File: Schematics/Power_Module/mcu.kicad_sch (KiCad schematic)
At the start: 38 parts, among them J5 USB_C_Female_USB2_Small, J6 SWD_B, J7 Stack Male Edge Connector, SW1 SW_STM_RESET, SW2 SW_STM_BOOT_MODE, U13 CP2102N-A02-GQFN20R, U14 STM32F103CBT6, U15 ISO1044BDR, U16 W25Q128JVS, Y1 X322516MMB4SI

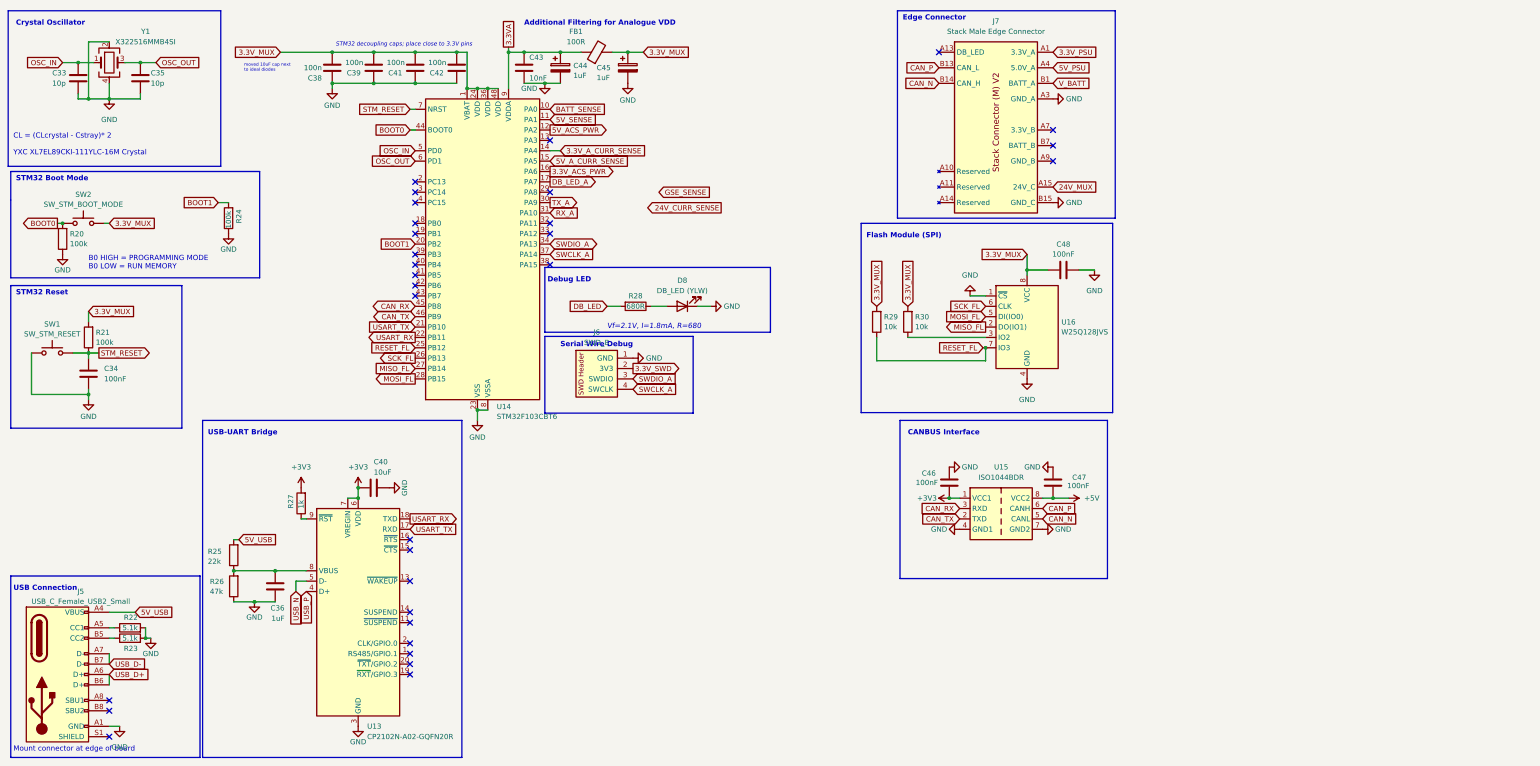
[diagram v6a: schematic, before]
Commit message: major layout progress, still need to place MCU
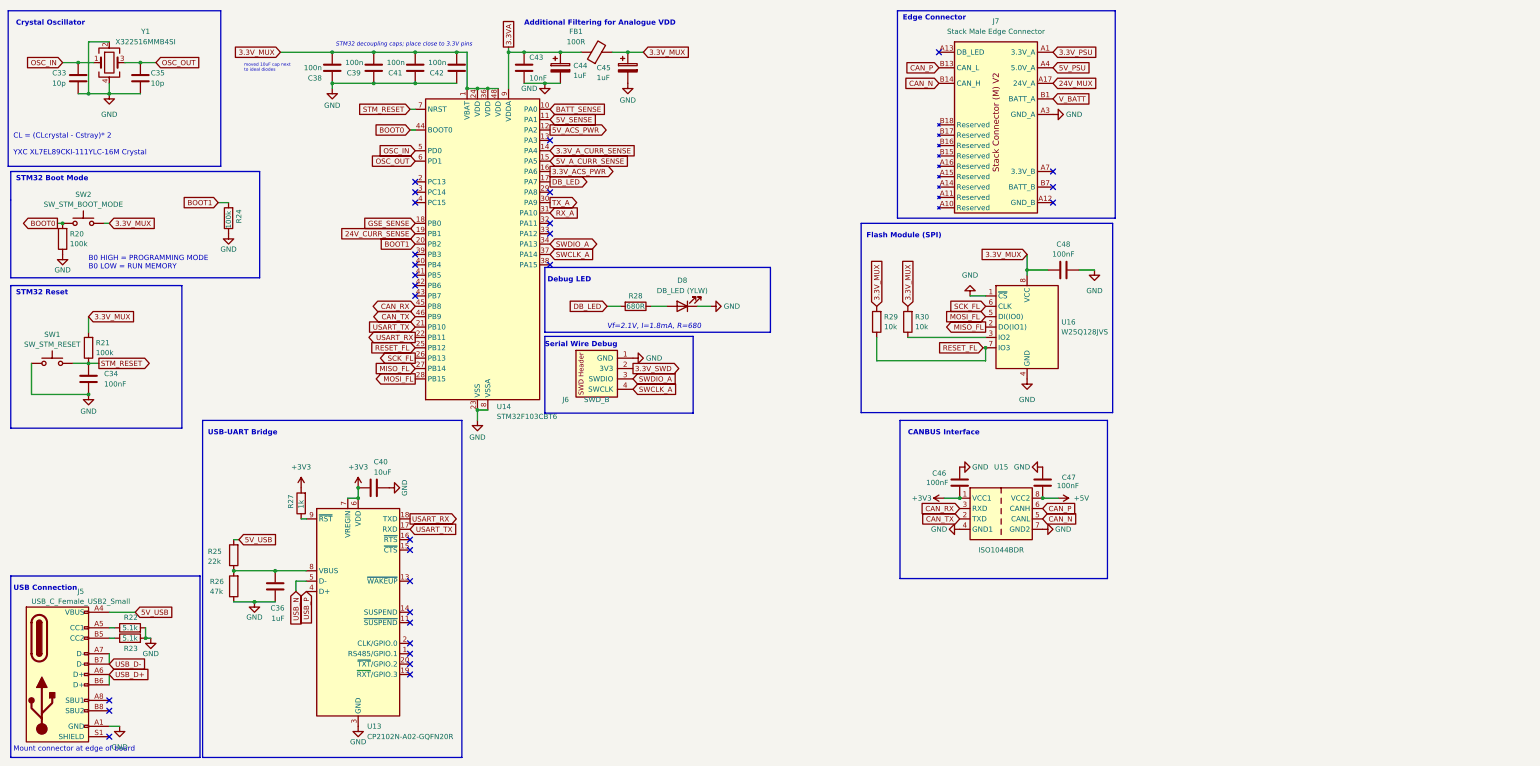
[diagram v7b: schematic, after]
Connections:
- net DB_LED_A is gone; now on net DB_LED: U14.17 (PA7)
- net 24V_CURR_SENSE: now also U14.19 (PB1)
- net 24V_MUX: no longer J7.A15 (24V_C), J7.A16 (24V_C)
- net GND: no longer J7.B15 (GND_C), J7.B16 (GND_C), J7.B17 (GND_C), J7.B18 (GND_C)
- net GSE_SENSE: now also U14.18 (PB0)
- no-connect marks 31 -> 29
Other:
- moved on the sheet: C34, C46, C47, R21, SW1

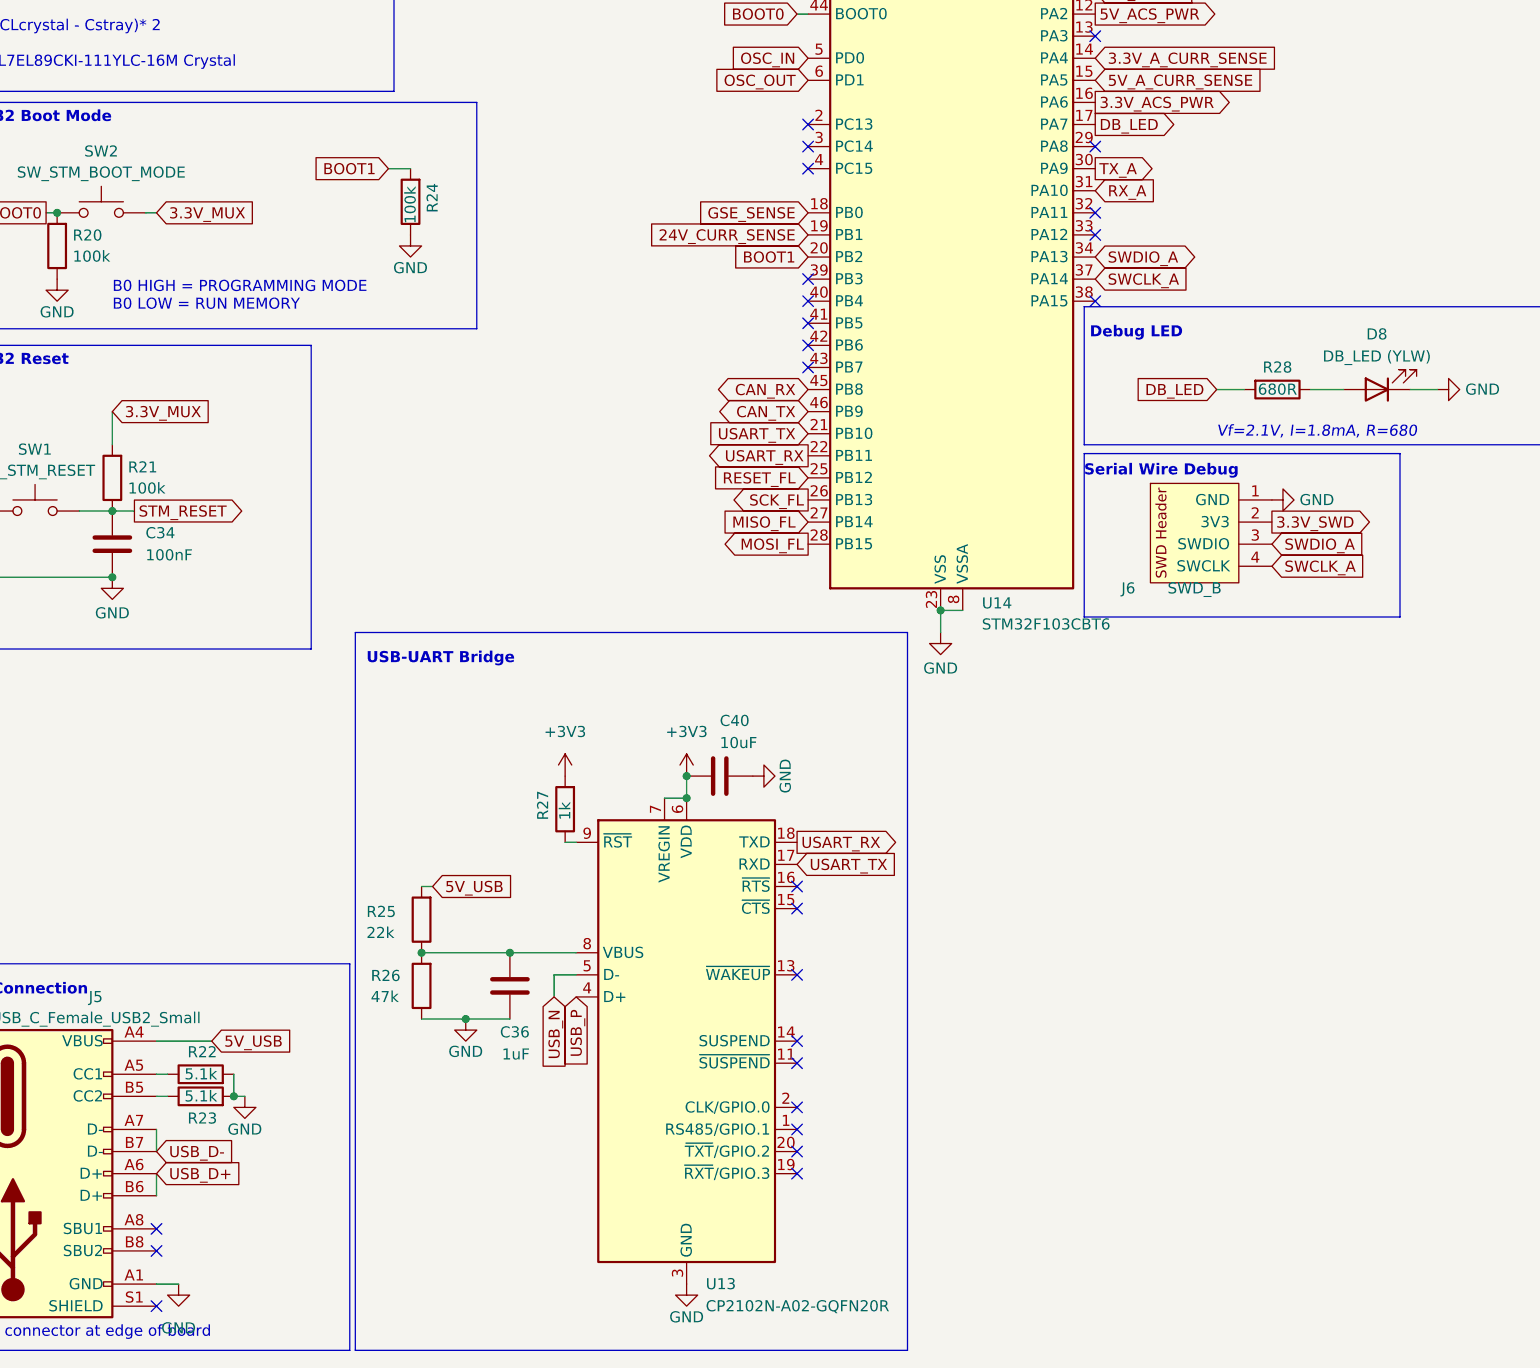
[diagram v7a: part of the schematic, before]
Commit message: continueing layout, confirmed all devices will fix  - need to add bulk rail caps  - fixed issue in oring logic
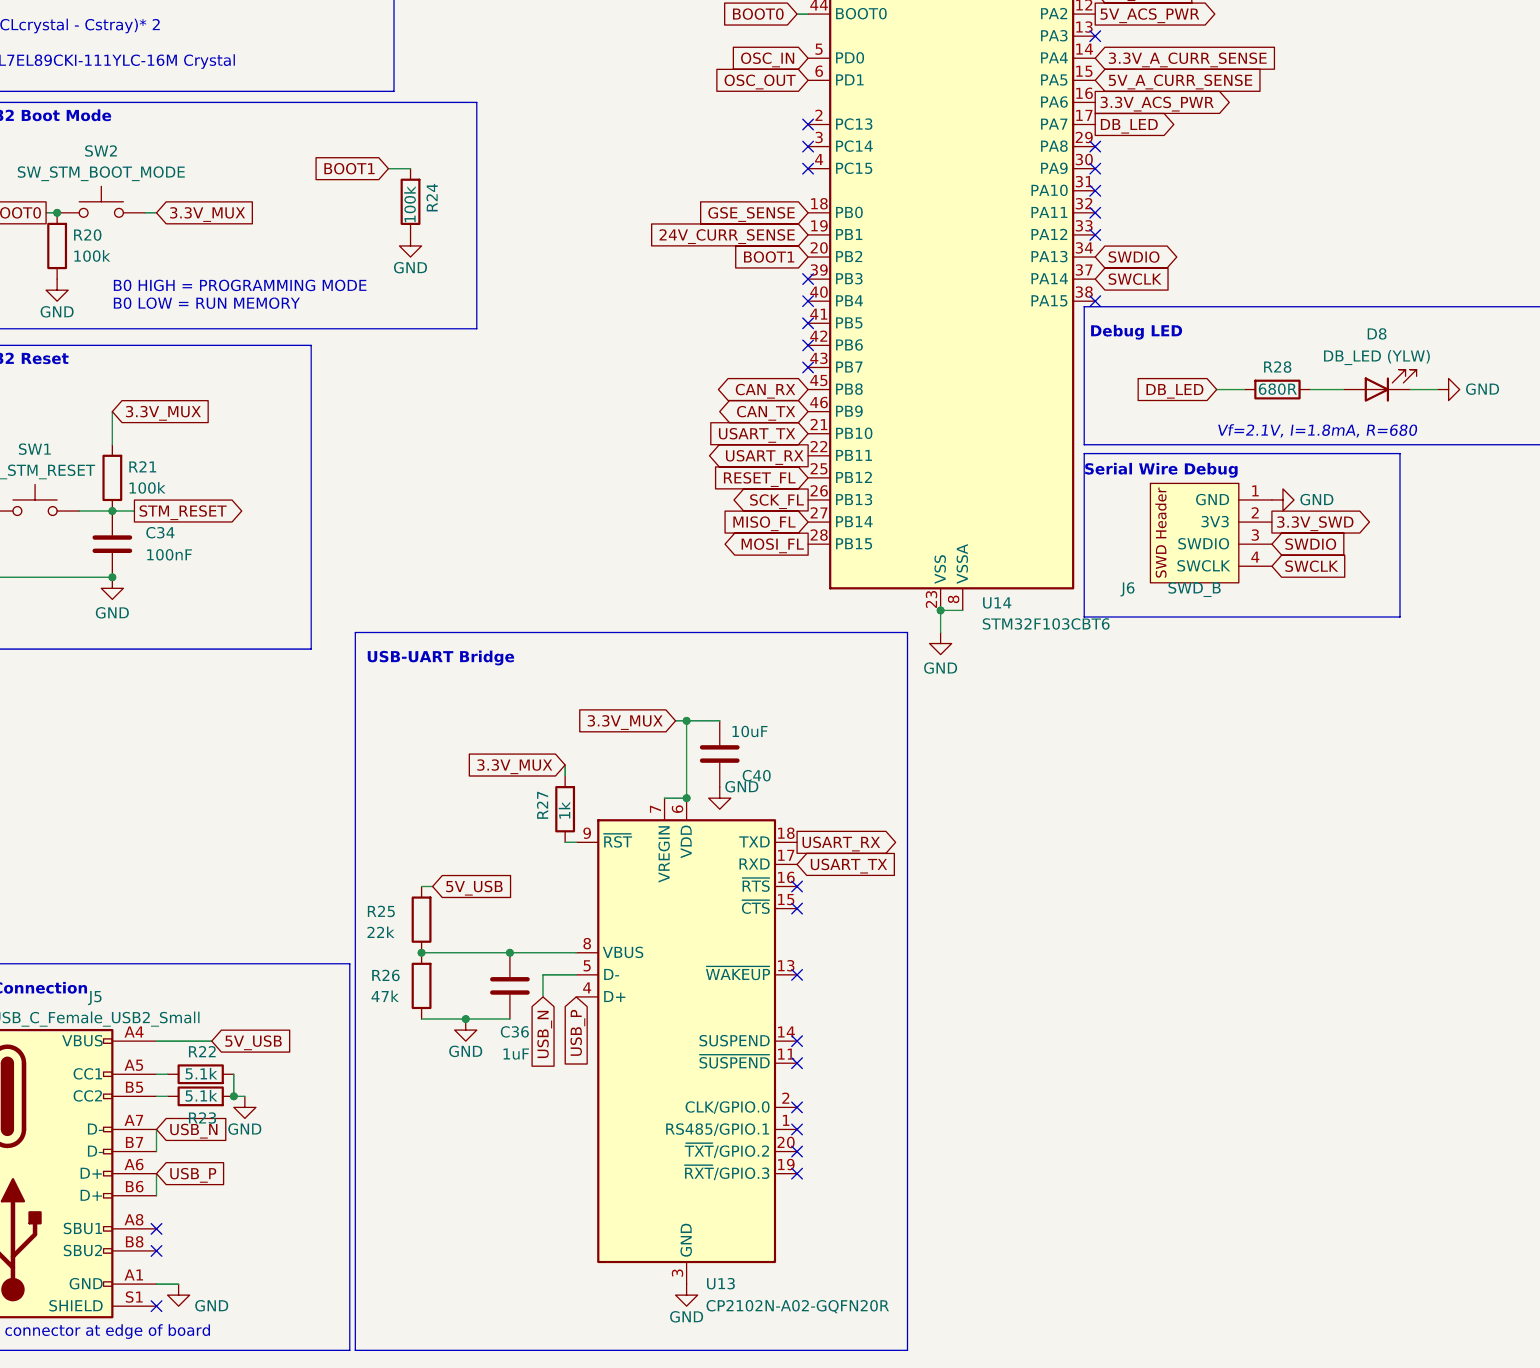
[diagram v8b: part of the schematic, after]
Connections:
- net USB_D+ is gone; now on net USB_P: J5.A6 (D+), J5.B6 (D+)
- net USB_D- is gone; now on net USB_N: J5.A7 (D-), J5.B7 (D-)
- net +3V3: no longer C40.2, R27.2, U13.6 (VDD), U13.7 (VREGIN)
- net 3.3V_MUX: now also C40.1, R27.2, U13.6 (VDD), U13.7 (VREGIN)
- net GND: now also C40.2; no longer C40.1
- net RX_A: no longer names the net of U14.31 (PA10)
- net SWCLK_A renamed SWCLK
- net SWDIO_A renamed SWDIO
- net TX_A: no longer names the net of U14.30 (PA9)
- no-connect marks 29 -> 31
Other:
- moved on the sheet: C40
